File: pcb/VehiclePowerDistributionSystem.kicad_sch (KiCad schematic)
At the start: 30 parts, among them J1 B4B-XH-A, J2 B4B-XH-A, J3 B4B-XH-A, J4 B8B-XH-A, J5 B2B-XH-A, J6 FFC2B28-24-G, J7 B2B-XH-A, J8 B2B-XH-A, U4 D24V7F5, U5 D24V7F3, U6 TPS22810DRV, U7 TPS22810DRV

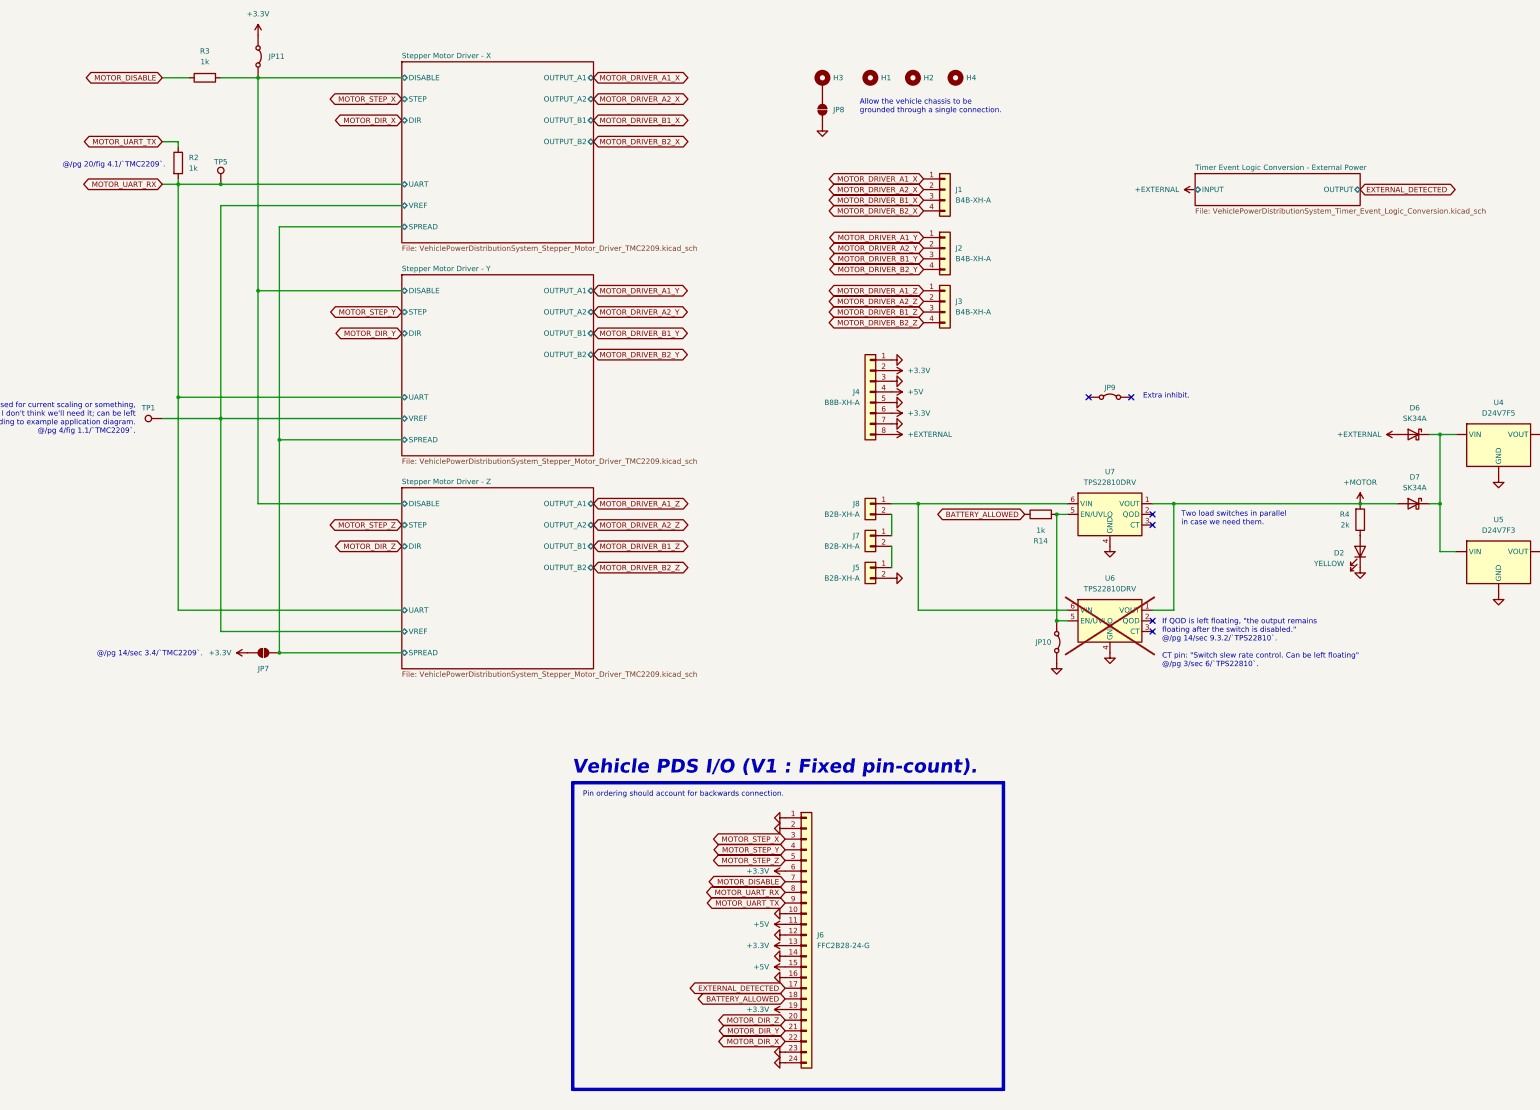
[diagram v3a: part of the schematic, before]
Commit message: Made `VehicleFlightComputer` target and corrected nets for the STM32H533VET6 on `VehicleFlightComputer` PCB.
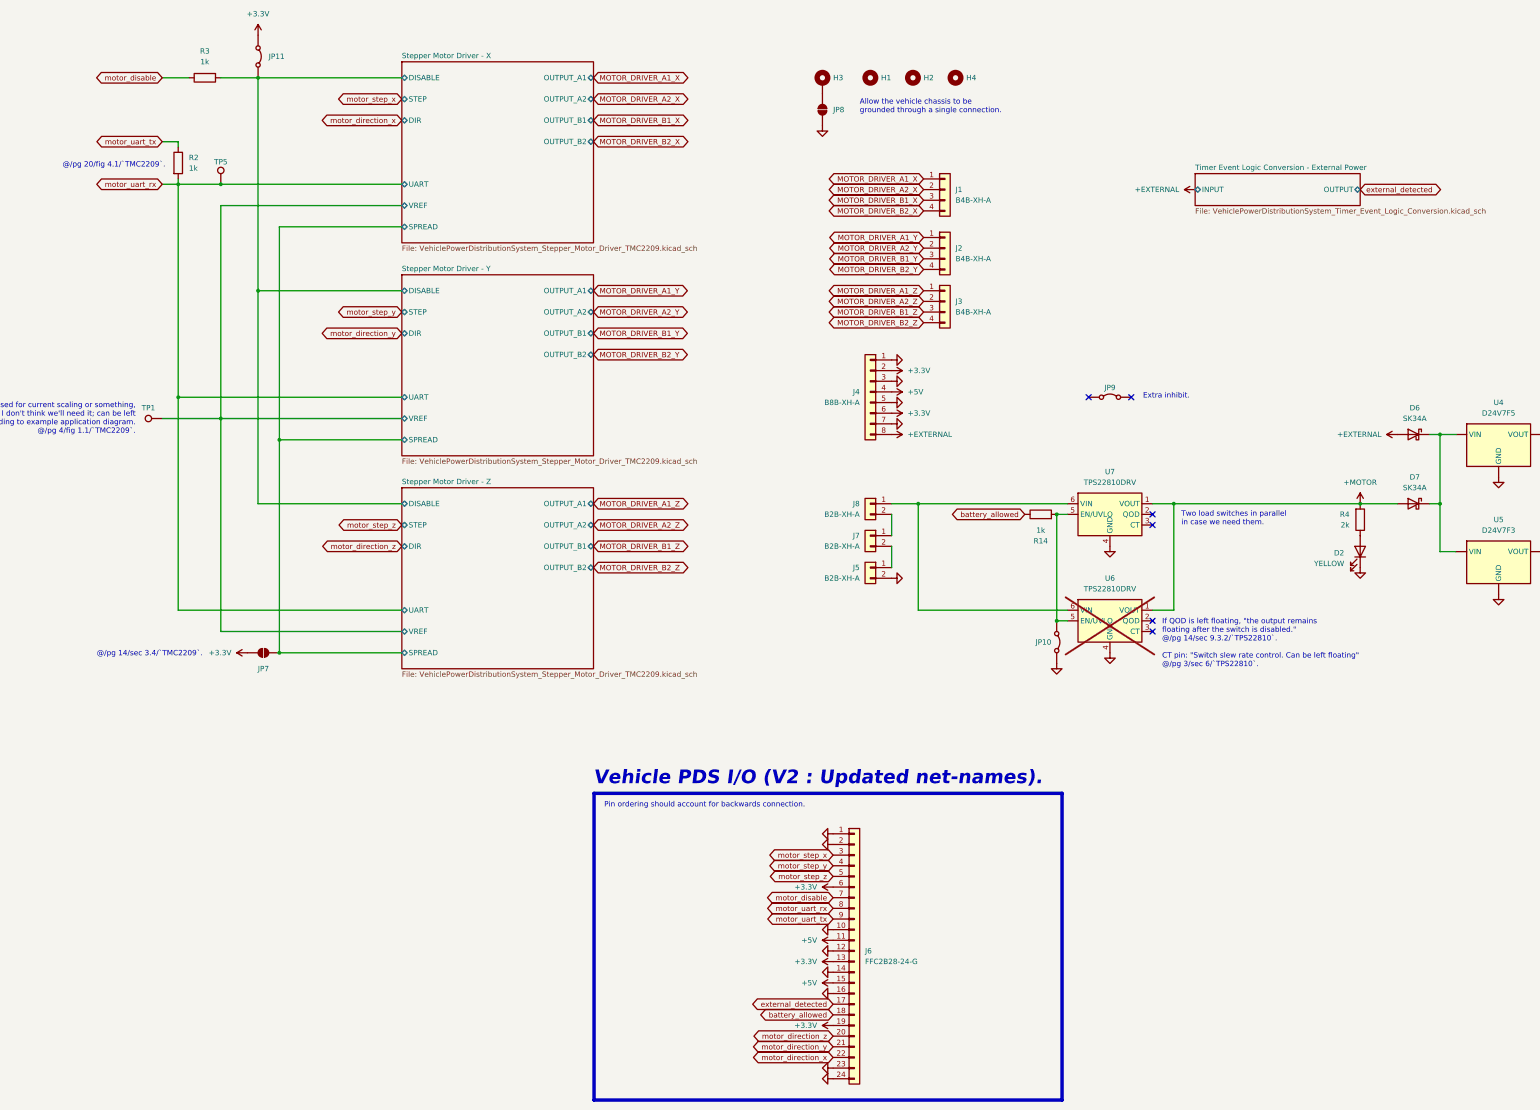
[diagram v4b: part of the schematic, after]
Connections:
- net BATTERY_ALLOWED renamed battery_allowed
- net EXTERNAL_DETECTED renamed external_detected
- net MOTOR_DIR_X renamed motor_direction_x
- net MOTOR_DIR_Y renamed motor_direction_y
- net MOTOR_DIR_Z renamed motor_direction_z
- net MOTOR_DISABLE renamed motor_disable
- net MOTOR_STEP_X renamed motor_step_x
- net MOTOR_STEP_Y renamed motor_step_y
- net MOTOR_STEP_Z renamed motor_step_z
- net MOTOR_UART_RX renamed motor_uart_rx
- net MOTOR_UART_TX renamed motor_uart_tx
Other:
- note added: "Vehicle PDS I/O (V2 : Updated net-names)."
- note removed: "Vehicle PDS I/O (V1 : Fixed pin-count)."
- moved on the sheet: J6

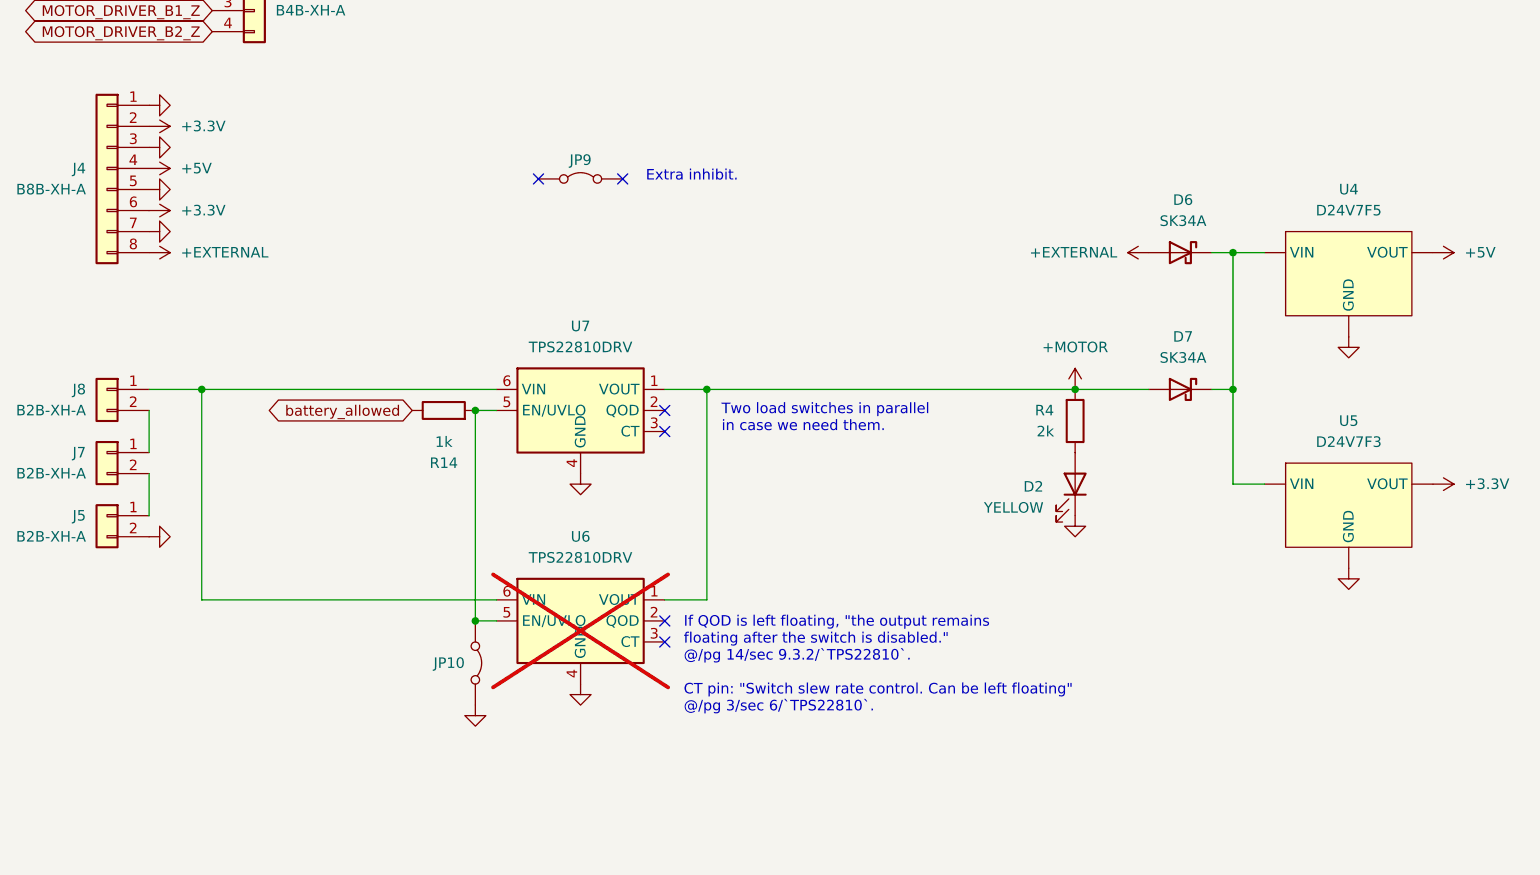
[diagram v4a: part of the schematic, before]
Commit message: Using `BTS462TATMA1` load-switch instead of `TPS22810DRV`.
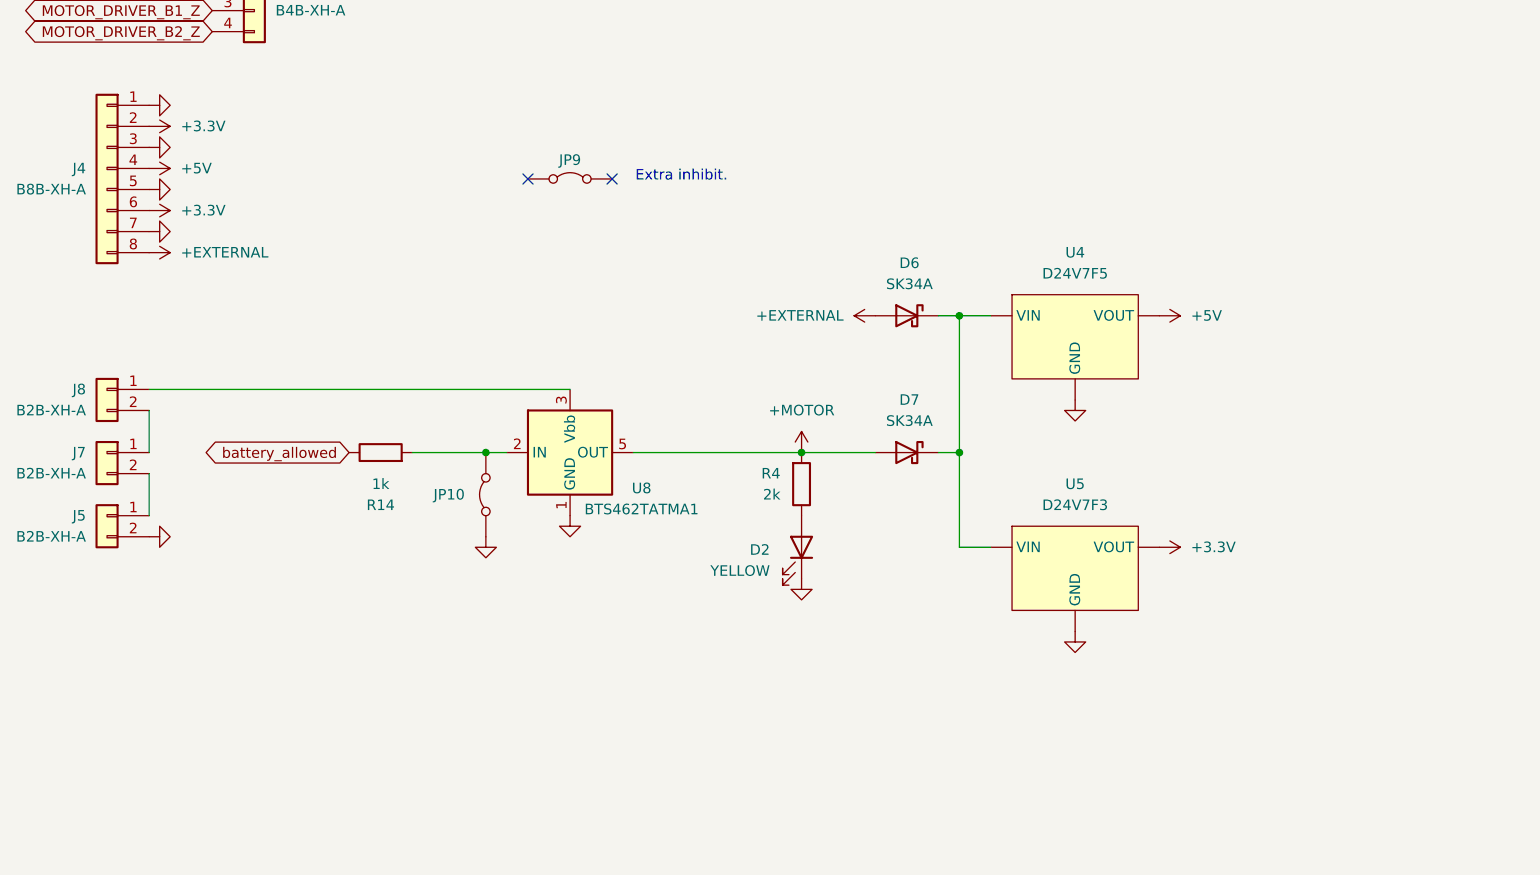
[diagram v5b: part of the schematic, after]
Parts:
- removed U6, U7: TPS22810DRV, Package_SON:WSON-6-1EP_2x2mm_P0.65mm_EP1x1.6mm_ThermalVias, symbol Power_Management:TPS22810DRV
- added U8: BTS462TATMA1, Package_TO_SOT_SMD:TO-252-4, symbol Power_Management:BTS462TATMA1
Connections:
- net +MOTOR: now also U8.5 (OUT)
- net GND: now also U8.1 (GND)
- net at JP10.2 (B), R14.2: now also U8.2 (IN)
- net at J8.1 (Pin_1): now also U8.3 (Vbb)
- no-connect marks 6 -> 2
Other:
- note removed: "If QOD is left floating, "the output remains floating after the switch is disabled." @/pg 14/sec 9.3.2/`TPS22810`. CT pin: "Switch slew rate control. Can be left floating" @/pg 3/sec 6/`TPS22810`."
- note removed: "Two load switches in parallel in case we need them."
- moved on the sheet: D2, D6, D7, JP10, JP9, R14, R4, U4, U5

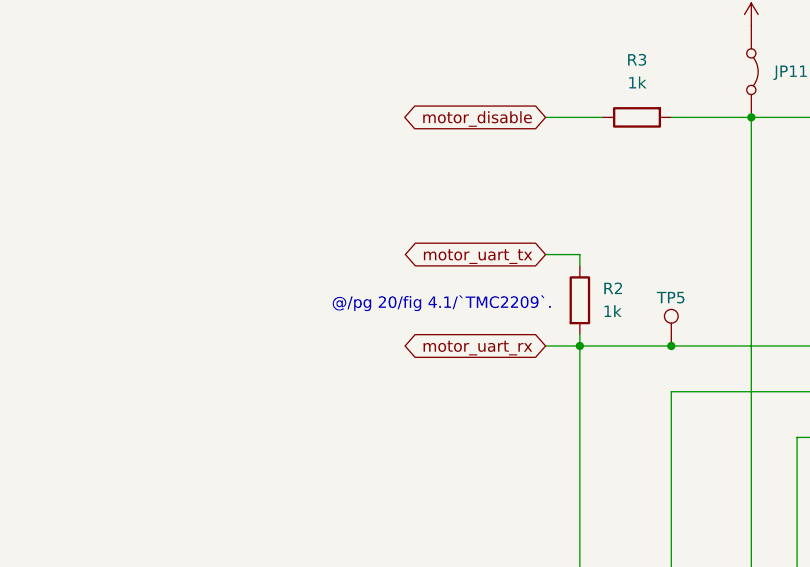
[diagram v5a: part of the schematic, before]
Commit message: Added pull-up resistor for UART line of TMC2209 drivers.
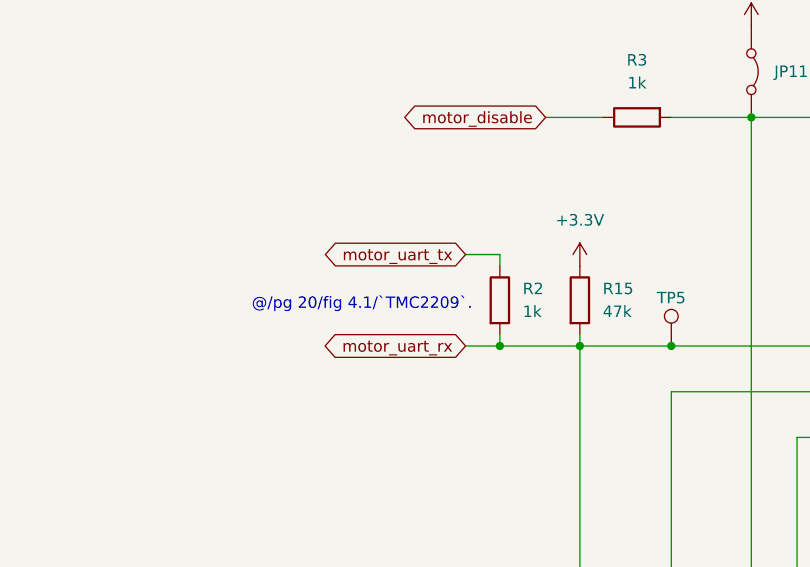
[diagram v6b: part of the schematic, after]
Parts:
- added R15: 47k, Resistor_SMD:R_1206_3216Metric_Pad1.30x1.75mm_HandSolder, symbol Device:R
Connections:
- net +3.3V: now also R15.1
- net motor_uart_rx: now also R15.2
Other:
- moved on the sheet: R2
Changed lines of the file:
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@@
 	(text "@/pg 20/fig 4.1/`TMC2209`."
 		(exclude_from_sim no)
-		(at 68.072 58.928 0)
+		(at 59.182 58.928 0)
 		(effects
 			(font
@@
 	)
 	(junction
+		(at 62.23 63.5)
+		(diameter 0)
+		(color 0 0 0 0)
+	)
+	(junction
 		(at 81.28 119.38)
 		(diameter 0)
@@
 	(wire
 		(pts
-			(xy 71.12 53.34) (xy 67.31 53.34)
+			(xy 62.23 53.34) (xy 58.42 53.34)
 		)
 		(stroke
@@
 	(wire
 		(pts
-			(xy 71.12 62.23) (xy 71.12 63.5)
+			(xy 62.23 62.23) (xy 62.23 63.5)
 		)
 		(stroke
@@
 	(wire
 		(pts
-			(xy 71.12 54.61) (xy 71.12 53.34)
+			(xy 62.23 54.61) (xy 62.23 53.34)
 		)
 		(stroke
@@
 	(wire
 		(pts
-			(xy 67.31 63.5) (xy 71.12 63.5)
+			(xy 58.42 63.5) (xy 62.23 63.5)
 		)
 		(stroke
@@
 	(wire
 		(pts
+			(xy 62.23 63.5) (xy 71.12 63.5)
+		)
+		(stroke
+			(width 0)
+			(type default)
+		)
+	)
+	(wire
+		(pts
 			(xy 124.46 88.9) (xy 90.17 88.9)
 		)
@@
 		)
 	)
+	(wire
+		(pts
+			(xy 71.12 62.23) (xy 71.12 63.5)
+		)
+		(stroke
+			(width 0)
+			(type default)
+		)
+	)
 	(global_label "MOTOR_DRIVER_A1_X"
 		(shape bidirectional)
@@
 	(global_label "motor_uart_rx"
 		(shape bidirectional)
-		(at 67.31 63.5 180)
+		(at 58.42 63.5 180)
 		(fields_autoplaced yes)
 		(effects
@@
 		)
 		(property "Intersheetrefs" "${INTERSHEET_REFS}"
-			(at 50.1509 63.5 0)
+			(at 41.2609 63.5 0)
 			(effects
 				(font
@@
 	(global_label "motor_uart_tx"
 		(shape bidirectional)
-		(at 67.31 53.34 180)
+		(at 58.42 53.34 180)
 		(fields_autoplaced yes)
 		(effects
@@
 		)
 		(property "Intersheetrefs" "${INTERSHEET_REFS}"
-			(at 50.2114 53.34 0)
+			(at 41.3214 53.34 0)
 			(effects
 				(font
@@
 	)
 	(symbol
+		(lib_id "Device:R")
+		(at 71.12 58.42 0)
+		(unit 1)
+		(exclude_from_sim no)
+		(in_bom yes)
+		(on_board yes)
+		(dnp no)
+		(fields_autoplaced yes)
+		(property "Reference" "R15"
+			(at 73.66 57.1499 0)
+			(effects
+				(font
+					(size 1.27 1.27)
+				)
+				(justify left)
+			)
+		)
+		(property "Value" "47k"
+			(at 73.66 59.6899 0)
+			(effects
+				(font
+					(size 1.27 1.27)
+				)
+				(justify left)
+			)
+		)
+		(property "Footprint" "Resistor_SMD:R_1206_3216Metric_Pad1.30x1.75mm_HandSolder"
+			(at 69.342 58.42 90)
+			(effects
+				(font
+					(size 1.27 1.27)
+				)
+				(hide yes)
+			)
+		)
+		(property "Datasheet" "~"
+			(at 71.12 58.42 0)
+			(effects
+				(font
+					(size 1.27 1.27)
+				)
+				(hide yes)
+			)
+		)
+		(property "Description" "Resistor"
+			(at 71.12 58.42 0)
+			(effects
+				(font
+					(size 1.27 1.27)
+				)
+				(hide yes)
+			)
+		)
+		(pin "1"
+		)
+		(pin "2"
+		)
+		(instances
+			(project "VehiclePowerDistributionSystem"
+				(path "/92a7a41c-8494-4e4b-ac2d-deb1f1cd8085"
+					(reference "R15")
+					(unit 1)
+				)
+			)
+		)
+	)
+	(symbol
 		(lib_id "Jumper:SolderJumper_2_Open")
 		(at 224.79 45.72 90)
@@
 	(symbol
 		(lib_id "Device:R")
-		(at 71.12 58.42 0)
+		(at 62.23 58.42 0)
 		(unit 1)
 		(exclude_from_sim no)
@@
 		(fields_autoplaced yes)
 		(property "Reference" "R2"
-			(at 73.66 57.1499 0)
+			(at 64.77 57.1499 0)
 			(effects
 				(font
@@
 		)
 		(property "Value" "1k"
-			(at 73.66 59.6899 0)
+			(at 64.77 59.6899 0)
 			(effects
 				(font
@@
 		)
 		(property "Footprint" "Resistor_SMD:R_1206_3216Metric_Pad1.30x1.75mm_HandSolder"
-			(at 69.342 58.42 90)
+			(at 60.452 58.42 90)
 			(effects
 				(font
@@
 		)
 		(property "Datasheet" "~"
-			(at 71.12 58.42 0)
+			(at 62.23 58.42 0)
 			(effects
 				(font
@@
 		)
 		(property "Description" "Resistor"
-			(at 71.12 58.42 0)
+			(at 62.23 58.42 0)
 			(effects
 				(font
@@
 					(unit 1)
 				)
+			)
+		)
+	)
+	(symbol
+		(lib_id "power:+3.3V")
+		(at 71.12 54.61 0)
+		(unit 1)
+		(exclude_from_sim no)
+		(in_bom yes)
+		(on_board yes)
+		(dnp no)
+		(fields_autoplaced yes)
+		(property "Reference" "#PWR011"
+			(at 71.12 58.42 0)
+			(effects
+				(font
+					(size 1.27 1.27)
+				)
+				(hide yes)
+			)
+		)
+		(property "Value" "+3.3V"
+			(at 71.12 49.53 0)
+			(effects
+				(font
+					(size 1.27 1.27)
+				)
+			)
+		)
+		(property "Footprint" ""
+			(at 71.12 54.61 0)
+			(effects
+				(font
+					(size 1.27 1.27)
+				)
+				(hide yes)
+			)
+		)
+		(property "Datasheet" ""
+			(at 71.12 54.61 0)
+			(effects
+				(font
+					(size 1.27 1.27)
+				)
+				(hide yes)
+			)
+		)
+		(property "Description" "Power symbol creates a global label with name \"+3.3V\""
+			(at 71.12 54.61 0)
+			(effects
+				(font
+					(size 1.27 1.27)
+				)
+				(hide yes)
+			)
+		)
+		(pin "1"
+		)
+		(instances
+			(project "VehiclePowerDistributionSystem"
+				(path "/92a7a41c-8494-4e4b-ac2d-deb1f1cd8085"
+					(reference "#PWR011")
+					(unit 1)
+				)
